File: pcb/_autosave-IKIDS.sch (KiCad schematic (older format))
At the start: 25 parts, among them U1 Elite-C

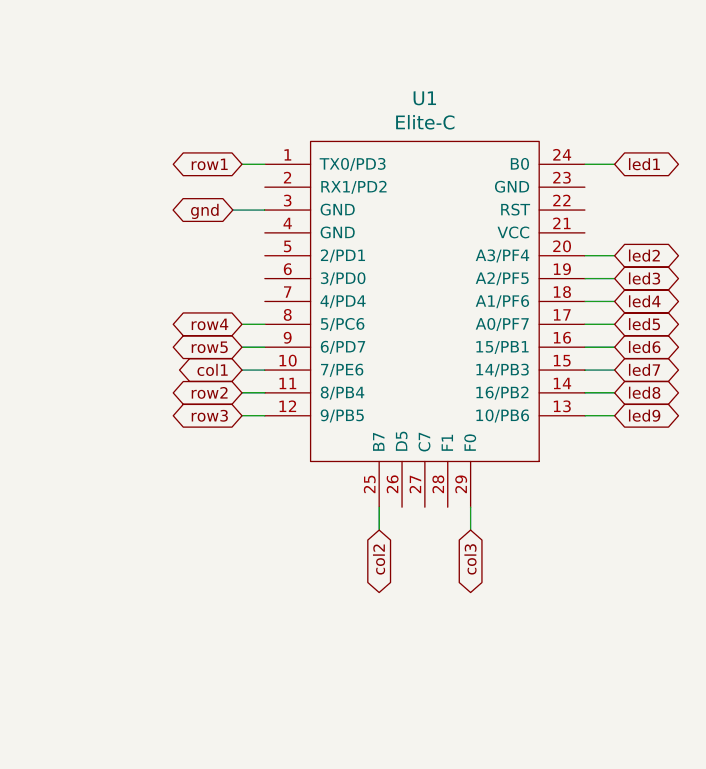
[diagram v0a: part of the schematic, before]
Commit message: Hooked up top 3 LEDs
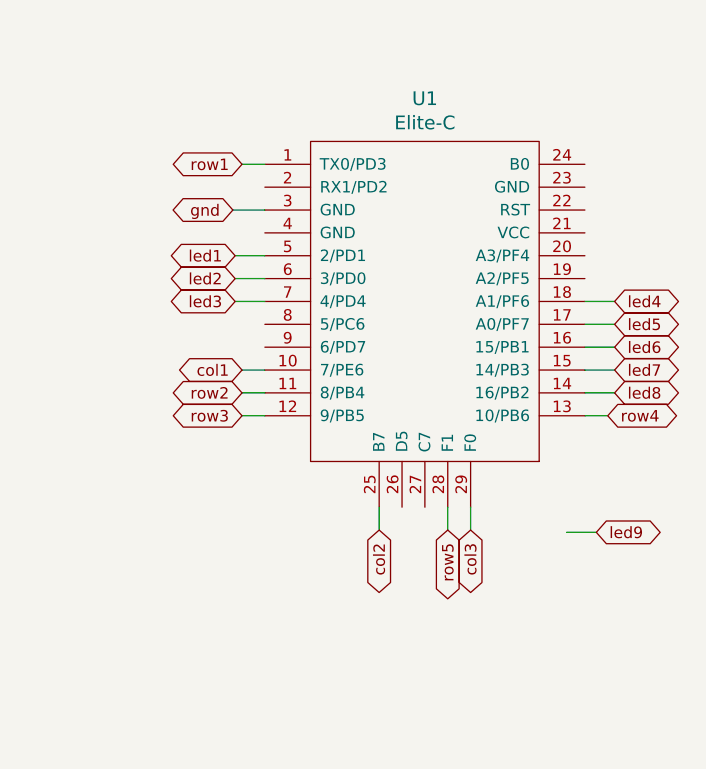
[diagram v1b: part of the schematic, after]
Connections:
- net led1: now also U1.5 (2/PD1); no longer U1.24 (B0)
- net led2: now also U1.6 (3/PD0); no longer U1.20 (A3/PF4)
- net led3: now also U1.7 (4/PD4); no longer U1.19 (A2/PF5)
- net led9: no longer U1.13 (10/PB6)
- net row4: now also U1.13 (10/PB6); no longer U1.8 (5/PC6)
- net row5: now also U1.28 (F1); no longer U1.9 (6/PD7)
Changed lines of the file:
@@
 Wire Wire Line
 	8730 3500 8830 3500
-Text GLabel 8730 3200 0    50   BiDi ~ 0
+Text GLabel 10330 3600 2    50   BiDi ~ 0
 row4
 Wire Wire Line
-	8730 3200 8830 3200
-Text GLabel 8730 3300 0    50   BiDi ~ 0
+	10330 3600 10230 3600
+Text GLabel 9630 4100 3    50   BiDi ~ 0
 row5
 Wire Wire Line
-	8730 3300 8830 3300
+	9630 4100 9630 4000
 Text GLabel 8730 3400 0    50   BiDi ~ 0
 col1
@@
 Wire Wire Line
 	6650 2530 6730 2530
-Text GLabel 10360 2500 2    50   BiDi ~ 0
+Text GLabel 8700 2900 0    50   BiDi ~ 0
 led1
-Text GLabel 10360 2900 2    50   BiDi ~ 0
+Text GLabel 8700 3000 0    50   BiDi ~ 0
 led2
-Text GLabel 10360 3000 2    50   BiDi ~ 0
+Text GLabel 8700 3100 0    50   BiDi ~ 0
 led3
 Text GLabel 10360 3100 2    50   BiDi ~ 0
@@
 Text GLabel 10360 3500 2    50   BiDi ~ 0
 led8
-Text GLabel 10360 3600 2    50   BiDi ~ 0
+Text GLabel 10280 4110 2    50   BiDi ~ 0
 led9
 Wire Wire Line
-	10360 3600 10230 3600
+	10280 4110 10150 4110
 Wire Wire Line
 	10230 3500 10360 3500
@@
 	10230 3100 10360 3100
 Wire Wire Line
-	10360 3000 10230 3000
-Wire Wire Line
-	10360 2900 10230 2900
-Wire Wire Line
-	10230 2500 10360 2500
+	8700 3100 8830 3100
+Wire Wire Line
+	8700 3000 8830 3000
+Wire Wire Line
+	8830 2900 8700 2900
 Wire Wire Line
 	8730 3600 8830 3600
